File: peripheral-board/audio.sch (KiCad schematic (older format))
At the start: 1 part

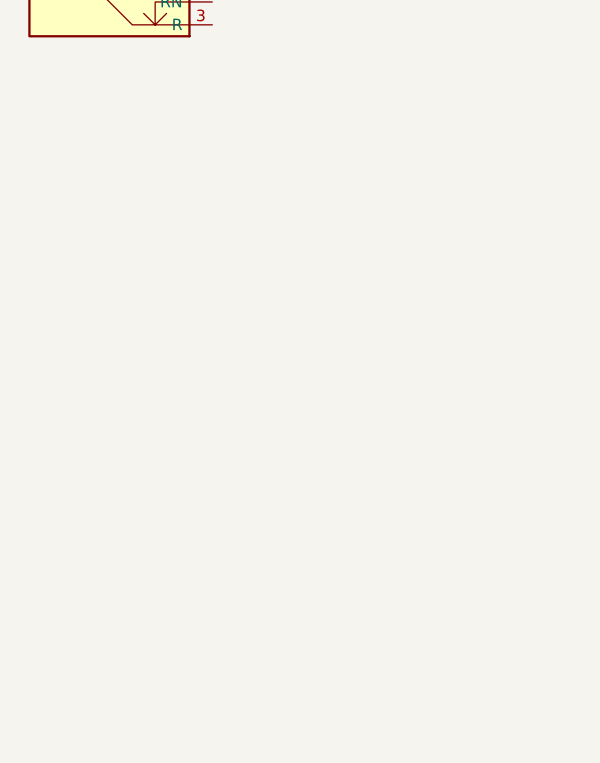
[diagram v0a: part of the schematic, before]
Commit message: added tac switch footprint
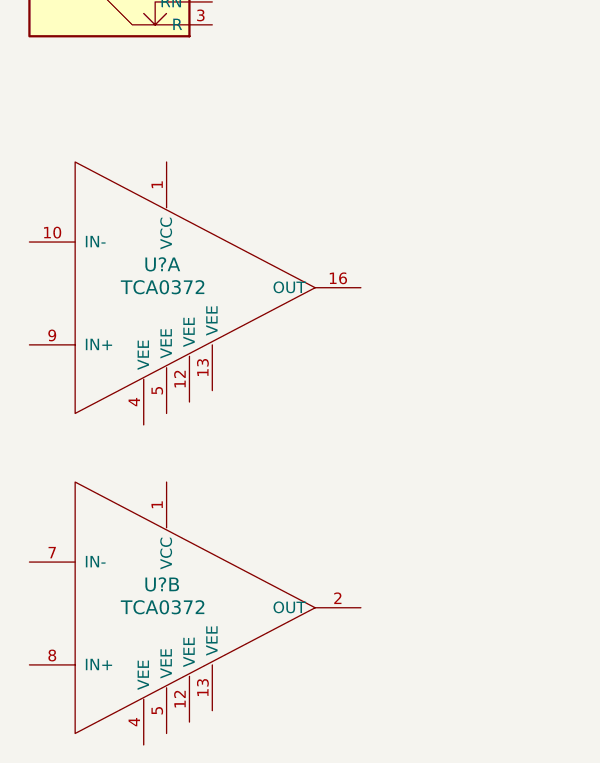
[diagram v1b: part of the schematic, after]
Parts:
- added U? (x2): TCA0372, symbol TCA0372
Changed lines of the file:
@@
 LIBS:contrib
 LIBS:valves
+LIBS:amp
 LIBS:peripheral-board-cache
 EELAYER 25 0
@@
 Text Notes 6200 2250 0    60   ~ 0
 Digital pot\nAmp
+$Comp
+L TCA0372 U?
+U 1 1 581D2053
+P 4700 3700
+F 0 "U?" H 4600 3800 60  0000 L CNN
+F 1 "TCA0372" H 4500 3700 60  0000 L CNN
+F 2 "" H 4700 3700 60  0001 C CNN
+F 3 "" H 4700 3700 60  0001 C CNN
+	1    4700 3700
+	1    0    0    -1
+$EndComp
+$Comp
+L TCA0372 U?
+U 2 1 581D2125
+P 4700 5100
+F 0 "U?" H 4600 5200 60  0000 L CNN
+F 1 "TCA0372" H 4500 5100 60  0000 L CNN
+F 2 "" H 4700 5100 60  0001 C CNN
+F 3 "" H 4700 5100 60  0001 C CNN
+	2    4700 5100
+	1    0    0    -1
+$EndComp
 $EndSCHEMATC

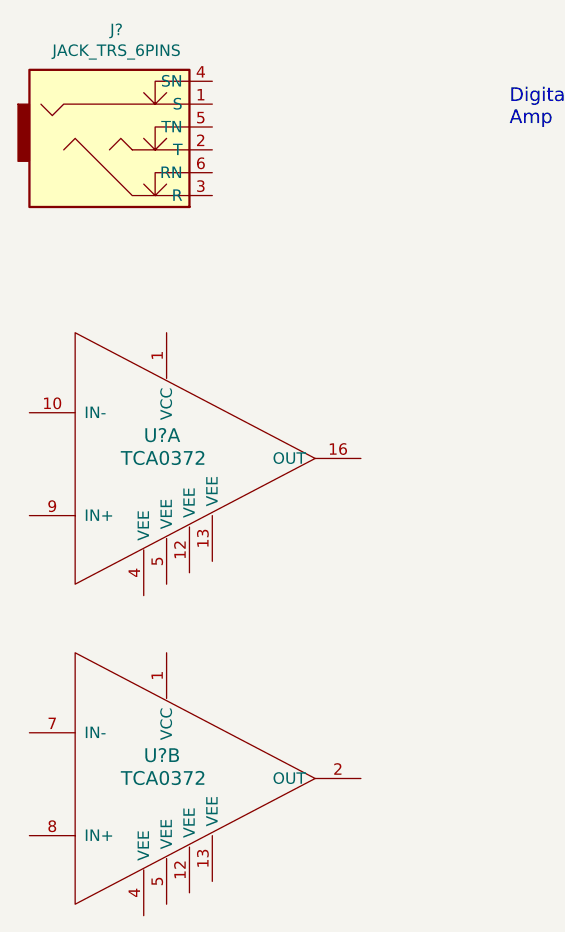
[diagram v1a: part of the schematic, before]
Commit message: added button 3d model
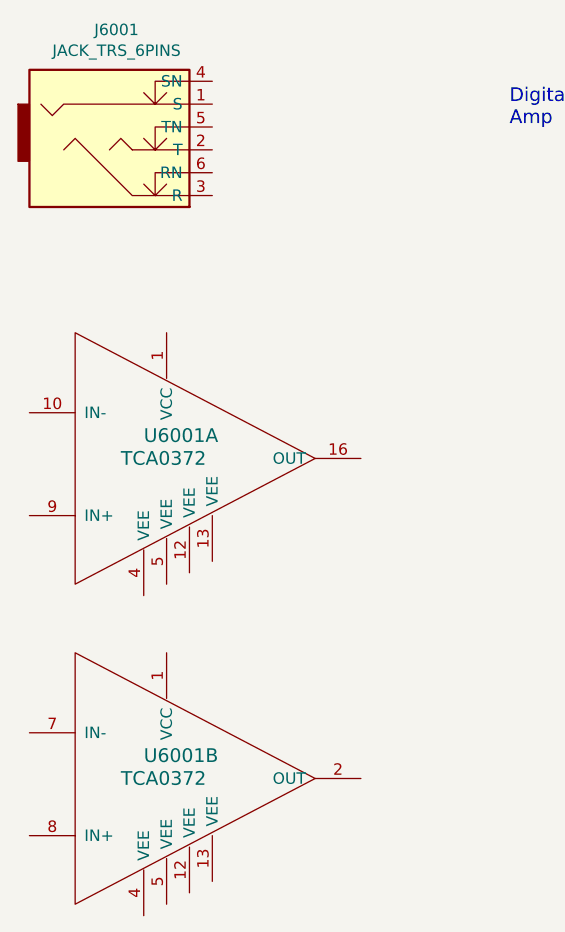
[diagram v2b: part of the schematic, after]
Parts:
- gave numbers to parts that had none: 2
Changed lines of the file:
@@
 $EndDescr
 $Comp
-L JACK_TRS_6PINS J?
+L JACK_TRS_6PINS J6001
 U 1 1 5819EF20
 P 4500 2350
-F 0 "J?" H 4481 2875 50  0000 C CNN
+F 0 "J6001" H 4481 2875 50  0000 C CNN
 F 1 "JACK_TRS_6PINS" H 4481 2784 50  0000 C CNN
-F 2 "" H 4600 2200 50  0000 C CNN
+F 2 "" H 4600 2200 50  0001 C CNN
 F 3 "" H 4600 2200 50  0000 C CNN
 	1    4500 2350
@@
 Digital pot\nAmp
 $Comp
-L TCA0372 U?
+L TCA0372 U6001
 U 1 1 581D2053
 P 4700 3700
-F 0 "U?" H 4600 3800 60  0000 L CNN
+F 0 "U6001" H 4600 3800 60  0000 L CNN
 F 1 "TCA0372" H 4500 3700 60  0000 L CNN
 F 2 "" H 4700 3700 60  0001 C CNN
@@
 $EndComp
 $Comp
-L TCA0372 U?
+L TCA0372 U6001
 U 2 1 581D2125
 P 4700 5100
-F 0 "U?" H 4600 5200 60  0000 L CNN
+F 0 "U6001" H 4600 5200 60  0000 L CNN
 F 1 "TCA0372" H 4500 5100 60  0000 L CNN
 F 2 "" H 4700 5100 60  0001 C CNN

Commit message: added peripheral board bus header
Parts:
- U6001: footprint (none) -> Housings_SOIC:SOIC-16_7.5x10.3mm_Pitch1.27mm
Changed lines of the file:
@@
 F 0 "U6001" H 4600 3800 60  0000 L CNN
 F 1 "TCA0372" H 4500 3700 60  0000 L CNN
-F 2 "" H 4700 3700 60  0001 C CNN
+F 2 "Housings_SOIC:SOIC-16_7.5x10.3mm_Pitch1.27mm" H 4700 3700 60  0001 C CNN
 F 3 "" H 4700 3700 60  0001 C CNN
 	1    4700 3700
@@
 F 0 "U6001" H 4600 5200 60  0000 L CNN
 F 1 "TCA0372" H 4500 5100 60  0000 L CNN
-F 2 "" H 4700 5100 60  0001 C CNN
+F 2 "Housings_SOIC:SOIC-16_7.5x10.3mm_Pitch1.27mm" H 4700 5100 60  0001 C CNN
 F 3 "" H 4700 5100 60  0001 C CNN
 	2    4700 5100

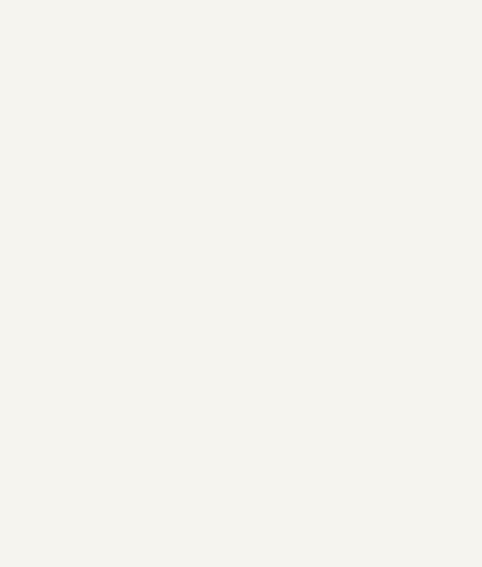
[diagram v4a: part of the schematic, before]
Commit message: routed keyboard
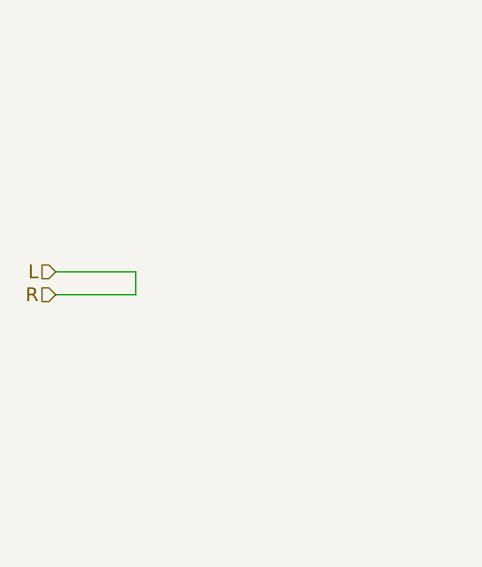
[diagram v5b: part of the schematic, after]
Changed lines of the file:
@@
 LIBS:amp
 LIBS:card-edge
+LIBS:switchmode
+LIBS:joystick
 LIBS:peripheral-board-cache
 EELAYER 25 0
@@
 	1    0    0    -1
 $EndComp
+Text HLabel 1800 3550 0    60   Input ~ 0
+L
+Text HLabel 1800 3650 0    60   Input ~ 0
+R
+Wire Wire Line
+	1800 3650 2150 3650
+Wire Wire Line
+	2150 3650 2150 3550
+Wire Wire Line
+	2150 3550 1800 3550
 $EndSCHEMATC

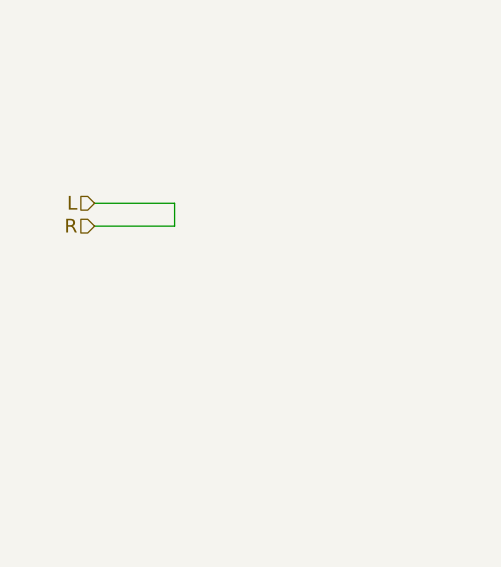
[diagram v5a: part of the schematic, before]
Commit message: some more keyboard stuff fit on this side..
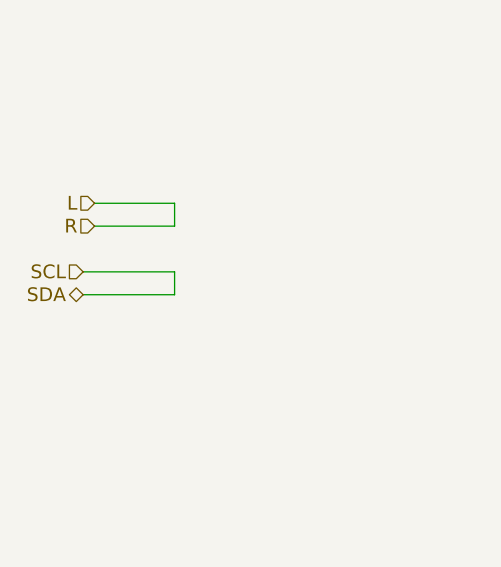
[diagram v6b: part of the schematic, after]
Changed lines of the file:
@@
 Wire Wire Line
 	2150 3550 1800 3550
+Text HLabel 1750 3950 0    60   BiDi ~ 0
+SDA
+Text HLabel 1750 3850 0    60   Input ~ 0
+SCL
+Wire Wire Line
+	1750 3850 2150 3850
+Wire Wire Line
+	2150 3850 2150 3950
+Wire Wire Line
+	2150 3950 1750 3950
 $EndSCHEMATC

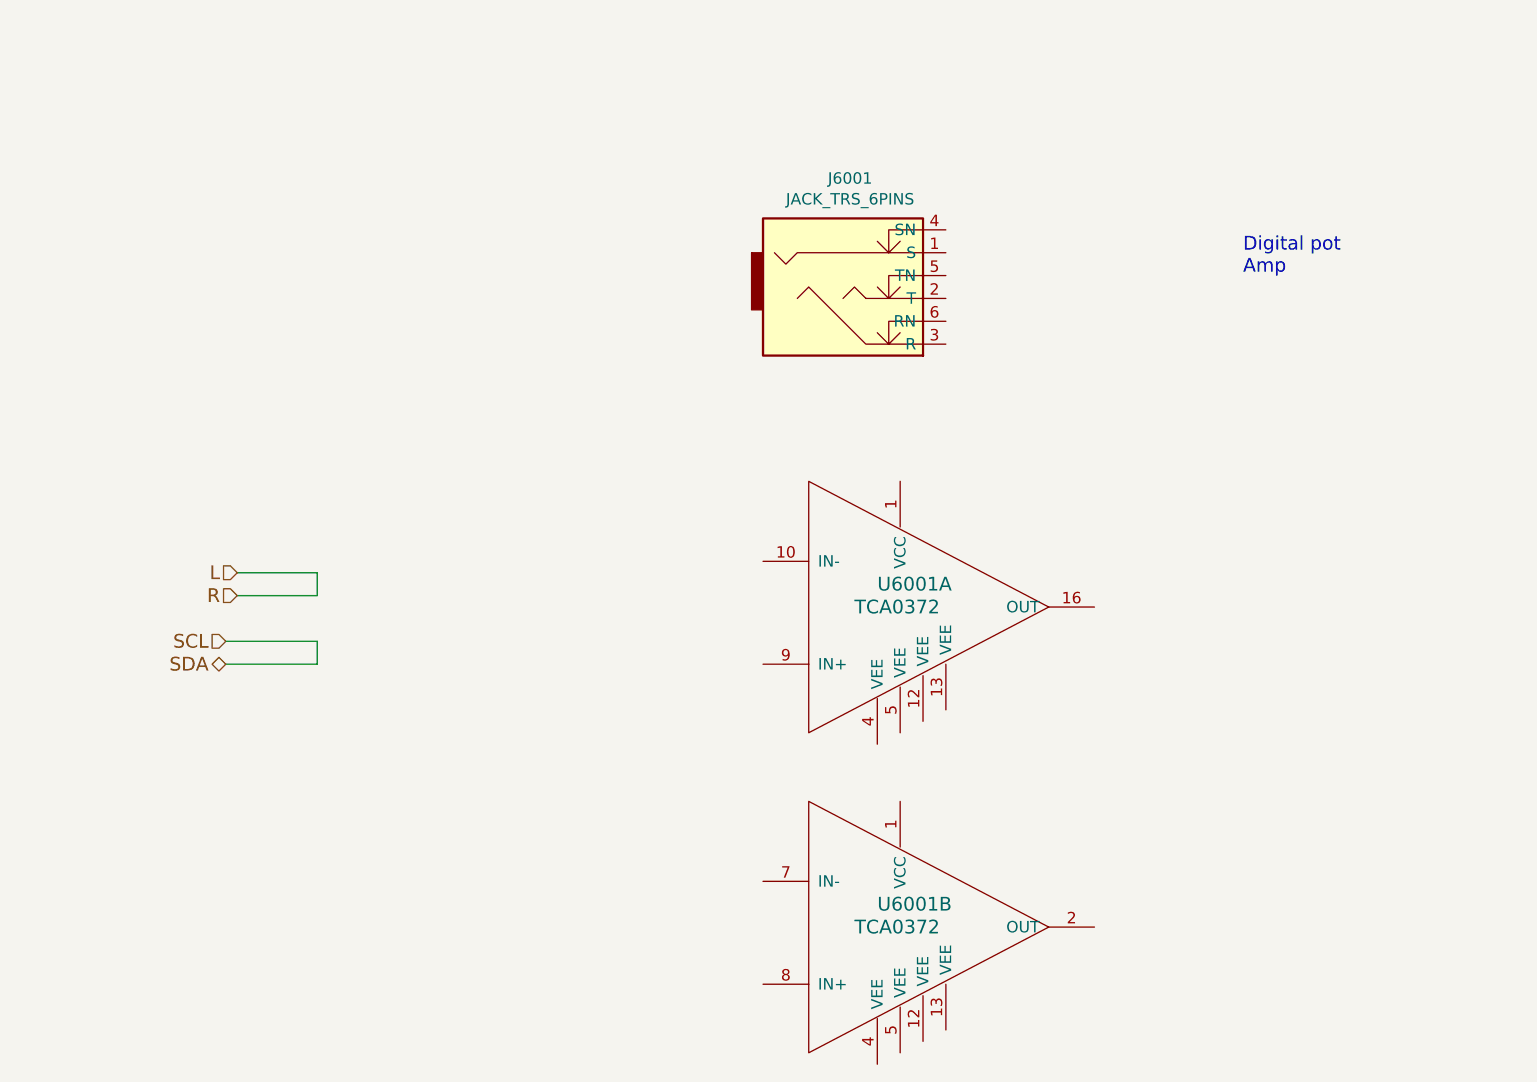
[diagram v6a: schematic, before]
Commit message: added some audio circuitry
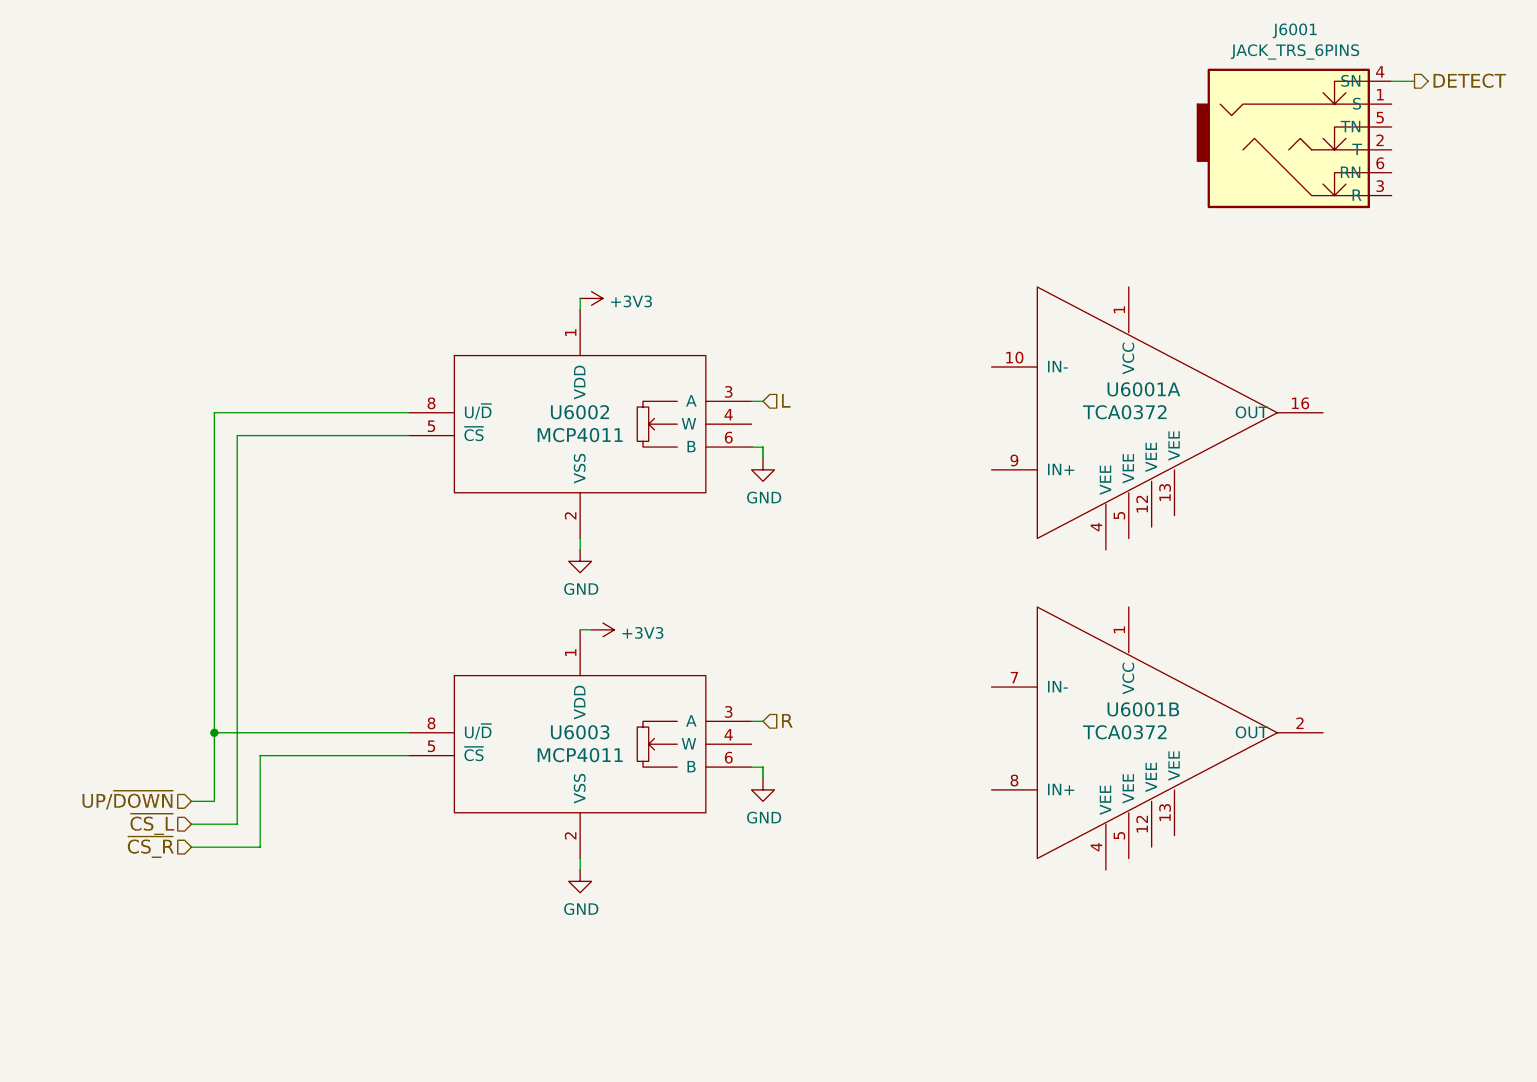
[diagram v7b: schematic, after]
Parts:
- added U6002, U6003: MCP4011, Housings_SOIC:SOIC-8_3.9x4.9mm_Pitch1.27mm, symbol MCP4011
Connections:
- net L: now also U6002.3 (A)
- net DETECT: now reaches J6001.4 (SN)
- new net +3V3: U6002.1 (VDD), U6003.1 (VDD)
- new net GND: U6002.2 (VSS), U6002.6 (B), U6003.2 (VSS), U6003.6 (B)
- new net R: U6003.3 (A)
- new net UP/~DOWN: U6002.8 (U/~D), U6003.8 (U/~D)
- new net ~CS_L: U6002.5 (~CS)
- new net ~CS_R: U6003.5 (~CS)
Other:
- note removed: "Digital pot\nAmp"
- moved on the sheet: J6001, U6001A, U6001B
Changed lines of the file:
@@
 LIBS:switchmode
 LIBS:joystick
+LIBS:digital-pot
 LIBS:peripheral-board-cache
-EELAYER 25 0
+EELAYER 26 0
 EELAYER END
 $Descr A4 11693 8268
@@
 L JACK_TRS_6PINS J6001
 U 1 1 5819EF20
-P 4500 2350
-F 0 "J6001" H 4481 2875 50  0000 C CNN
-F 1 "JACK_TRS_6PINS" H 4481 2784 50  0000 C CNN
-F 2 "" H 4600 2200 50  0001 C CNN
-F 3 "" H 4600 2200 50  0000 C CNN
-	1    4500 2350
+P 6450 1700
+F 0 "J6001" H 6431 2225 50  0000 C CNN
+F 1 "JACK_TRS_6PINS" H 6431 2134 50  0000 C CNN
+F 2 "" H 6550 1550 50  0001 C CNN
+F 3 "" H 6550 1550 50  0000 C CNN
+	1    6450 1700
 	1    0    0    -1
 $EndComp
-Text Notes 6200 2250 0    60   ~ 0
-Digital pot\nAmp
 $Comp
 L TCA0372 U6001
 U 1 1 581D2053
-P 4700 3700
-F 0 "U6001" H 4600 3800 60  0000 L CNN
-F 1 "TCA0372" H 4500 3700 60  0000 L CNN
-F 2 "Housings_SOIC:SOIC-16_7.5x10.3mm_Pitch1.27mm" H 4700 3700 60  0001 C CNN
-F 3 "" H 4700 3700 60  0001 C CNN
-	1    4700 3700
+P 5700 2850
+F 0 "U6001" H 5600 2950 60  0000 L CNN
+F 1 "TCA0372" H 5500 2850 60  0000 L CNN
+F 2 "Housings_SOIC:SOIC-16_7.5x10.3mm_Pitch1.27mm" H 5700 2850 60  0001 C CNN
+F 3 "" H 5700 2850 60  0001 C CNN
+	1    5700 2850
 	1    0    0    -1
 $EndComp
@@
 L TCA0372 U6001
 U 2 1 581D2125
-P 4700 5100
-F 0 "U6001" H 4600 5200 60  0000 L CNN
-F 1 "TCA0372" H 4500 5100 60  0000 L CNN
-F 2 "Housings_SOIC:SOIC-16_7.5x10.3mm_Pitch1.27mm" H 4700 5100 60  0001 C CNN
-F 3 "" H 4700 5100 60  0001 C CNN
-	2    4700 5100
+P 5700 4250
+F 0 "U6001" H 5600 4350 60  0000 L CNN
+F 1 "TCA0372" H 5500 4250 60  0000 L CNN
+F 2 "Housings_SOIC:SOIC-16_7.5x10.3mm_Pitch1.27mm" H 5700 4250 60  0001 C CNN
+F 3 "" H 5700 4250 60  0001 C CNN
+	2    5700 4250
 	1    0    0    -1
 $EndComp
-Text HLabel 1800 3550 0    60   Input ~ 0
+Text HLabel 4100 2800 2    60   Input ~ 0
 L
-Text HLabel 1800 3650 0    60   Input ~ 0
+Text HLabel 4100 4200 2    60   Input ~ 0
 R
+Text HLabel 1600 4550 0    60   Input ~ 0
+UP/~DOWN
+Text HLabel 1600 4650 0    60   Input ~ 0
+~CS_L
+Text HLabel 1600 4750 0    60   Input ~ 0
+~CS_R
+$Comp
+L MCP4011 U6002
+U 1 1 582347E6
+P 3300 2900
+F 0 "U6002" H 3300 2950 60  0000 C CNN
+F 1 "MCP4011" H 3300 2850 60  0000 C CNN
+F 2 "Housings_SOIC:SOIC-8_3.9x4.9mm_Pitch1.27mm" H 3300 2900 60  0001 C CNN
+F 3 "" H 3300 2900 60  0001 C CNN
+	1    3300 2900
+	1    0    0    -1
+$EndComp
+$Comp
+L MCP4011 U6003
+U 1 1 58234B7F
+P 3300 4300
+F 0 "U6003" H 3300 4350 60  0000 C CNN
+F 1 "MCP4011" H 3300 4250 60  0000 C CNN
+F 2 "Housings_SOIC:SOIC-8_3.9x4.9mm_Pitch1.27mm" H 3300 4300 60  0001 C CNN
+F 3 "" H 3300 4300 60  0001 C CNN
+	1    3300 4300
+	1    0    0    -1
+$EndComp
 Wire Wire Line
-	1800 3650 2150 3650
+	1700 2850 2550 2850
 Wire Wire Line
-	2150 3650 2150 3550
+	1800 2950 2550 2950
 Wire Wire Line
-	2150 3550 1800 3550
-Text HLabel 1750 3950 0    60   BiDi ~ 0
-SDA
-Text HLabel 1750 3850 0    60   Input ~ 0
-SCL
+	1700 4250 2550 4250
 Wire Wire Line
-	1750 3850 2150 3850
+	2550 4350 1900 4350
 Wire Wire Line
-	2150 3850 2150 3950
+	1700 2850 1700 4550
 Wire Wire Line
-	2150 3950 1750 3950
+	1700 4550 1600 4550
+Connection ~ 1700 4250
+Wire Wire Line
+	1800 2950 1800 4650
+Wire Wire Line
+	1800 4650 1600 4650
+Wire Wire Line
+	1900 4350 1900 4750
+Wire Wire Line
+	1900 4750 1600 4750
+$Comp
+L GND #PWR028
+U 1 1 5823647F
+P 3300 3450
+F 0 "#PWR028" H 3300 3200 50  0001 C CNN
+F 1 "GND" H 3305 3277 50  0000 C CNN
+F 2 "" H 3300 3450 50  0000 C CNN
+F 3 "" H 3300 3450 50  0000 C CNN
+	1    3300 3450
+	1    0    0    -1
+$EndComp
+$Comp
+L GND #PWR029
+U 1 1 582364AF
+P 3300 4850
+F 0 "#PWR029" H 3300 4600 50  0001 C CNN
+F 1 "GND" H 3305 4677 50  0000 C CNN
+F 2 "" H 3300 4850 50  0000 C CNN
+F 3 "" H 3300 4850 50  0000 C CNN
+	1    3300 4850
+	1    0    0    -1
+$EndComp
+$Comp
+L +3V3 #PWR030
+U 1 1 582364E9
+P 3300 2350
+F 0 "#PWR030" H 3300 2200 50  0001 C CNN
+F 1 "+3V3" V 3315 2478 50  0000 L CNN
+F 2 "" H 3300 2350 50  0000 C CNN
+F 3 "" H 3300 2350 50  0000 C CNN
+	1    3300 2350
+	0    1    1    0
+$EndComp
+$Comp
+L +3V3 #PWR031
+U 1 1 58236543
+P 3350 3800
+F 0 "#PWR031" H 3350 3650 50  0001 C CNN
+F 1 "+3V3" V 3365 3928 50  0000 L CNN
+F 2 "" H 3350 3800 50  0000 C CNN
+F 3 "" H 3350 3800 50  0000 C CNN
+	1    3350 3800
+	0    1    1    0
+$EndComp
+Wire Wire Line
+	3300 2350 3300 2400
+Wire Wire Line
+	3300 3400 3300 3450
+Wire Wire Line
+	3300 3800 3350 3800
+Wire Wire Line
+	3300 4800 3300 4850
+Text HLabel 6950 1400 2    60   Output ~ 0
+DETECT
+Wire Wire Line
+	6950 1400 6850 1400
+Wire Wire Line
+	4100 4200 4050 4200
+Wire Wire Line
+	4100 2800 4050 2800
+$Comp
+L GND #PWR032
+U 1 1 58240DA5
+P 4100 3050
+F 0 "#PWR032" H 4100 2800 50  0001 C CNN
+F 1 "GND" H 4105 2877 50  0000 C CNN
+F 2 "" H 4100 3050 50  0000 C CNN
+F 3 "" H 4100 3050 50  0000 C CNN
+	1    4100 3050
+	1    0    0    -1
+$EndComp
+$Comp
+L GND #PWR033
+U 1 1 58240DD7
+P 4100 4450
+F 0 "#PWR033" H 4100 4200 50  0001 C CNN
+F 1 "GND" H 4105 4277 50  0000 C CNN
+F 2 "" H 4100 4450 50  0000 C CNN
+F 3 "" H 4100 4450 50  0000 C CNN
+	1    4100 4450
+	1    0    0    -1
+$EndComp
+Wire Wire Line
+	4100 4450 4100 4400
+Wire Wire Line
+	4100 4400 4050 4400
+Wire Wire Line
+	4050 3000 4100 3000
+Wire Wire Line
+	4100 3000 4100 3050
 $EndSCHEMATC
